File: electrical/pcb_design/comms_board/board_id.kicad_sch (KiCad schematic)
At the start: 10 parts

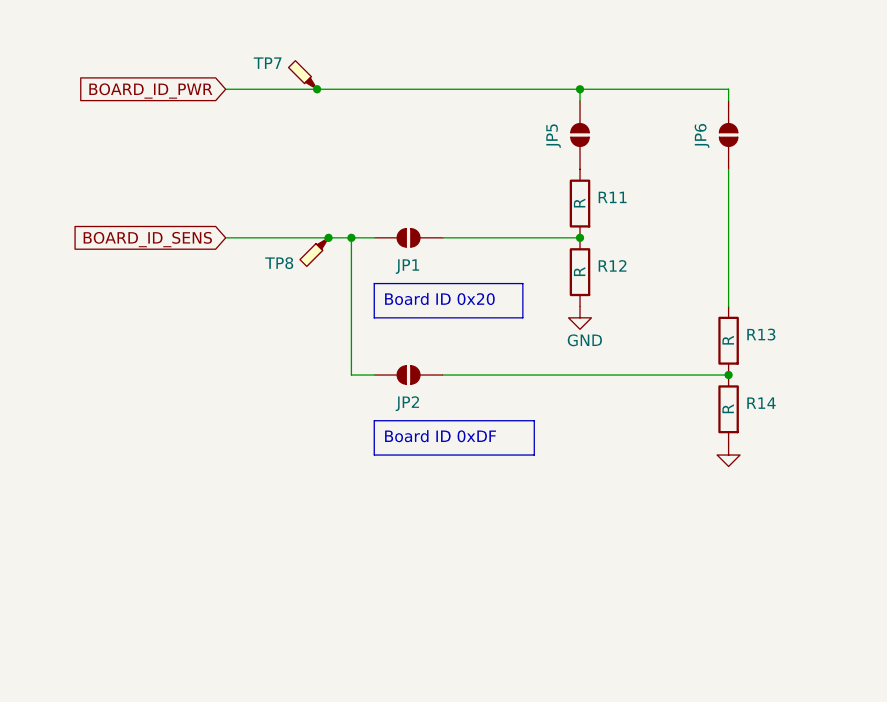
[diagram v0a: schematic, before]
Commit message: Create comms board for cheerful coffee edition based on magnetorquer control board
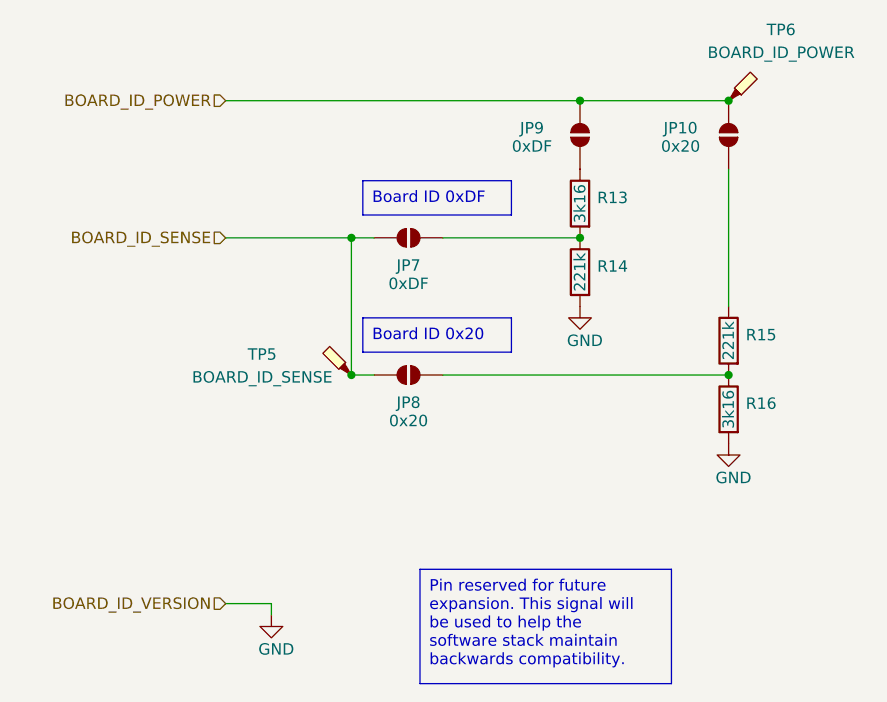
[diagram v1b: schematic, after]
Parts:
- removed JP2, JP6: SolderJumper_2_Open, Jumper:SolderJumper-2_P1.3mm_Open_RoundedPad1.0x1.5mm, symbol Jumper:SolderJumper_2_Open
- removed TP7, TP8: TestPoint_Probe, footprints:TestPoint_Pad_D2.5mm, symbol Connector:TestPoint_Probe
- added JP10, JP8: 0x20, Jumper:SolderJumper-2_P1.3mm_Open_RoundedPad1.0x1.5mm, symbol Jumper:SolderJumper_2_Open
- added TP5: BOARD_ID_SENSE, footprints:TestPoint_Pad_D1.5mm, symbol Connector:TestPoint_Probe
- added TP6: BOARD_ID_POWER, footprints:TestPoint_Pad_D1.5mm, symbol Connector:TestPoint_Probe
- JP7: renamed from JP1; value SolderJumper_2_Open -> 0xDF
- JP9: renamed from JP5; value SolderJumper_2_Open -> 0xDF
- R13: renamed from R11; value R -> 3k16; Active Y -> (none); MPN C11476 -> (none); Manufacturer Part Number 0402WGF1872TCE -> (none)
- R14: renamed from R12; value R -> 221k; Active Y -> (none); MPN C25914 -> (none); Manufacturer Part Number 0402WGF6191TCE -> (none)
- R15: renamed from R13; value R -> 221k; Active Y -> (none); MPN C25914 -> (none); Manufacturer Part Number 0402WGF6191TCE -> (none)
- R16: renamed from R14; value R -> 3k16; Active Y -> (none); MPN C11476 -> (none); Manufacturer Part Number 0402WGF1872TCE -> (none)
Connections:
- net at R15.1: now also JP10.2 (B)
- net at R15.2, R16.1: now also JP8.2 (B)
- net BOARD_ID_PWR renamed BOARD_ID_POWER
- net BOARD_ID_POWER: now also JP10.1 (A), TP6.1
- net BOARD_ID_SENS renamed BOARD_ID_SENSE
- net BOARD_ID_SENSE: now also JP8.1 (A), TP5.1

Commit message: Add missing part numbers to comms board.
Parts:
- R13, R16: Active (none) -> Y; Basic or Extended Component Basic -> Extended; MPN (none) -> C11462; Manufacturer Part Number (none) -> 0402WGF3161TCE
- R14, R15: Active (none) -> Y; Basic or Extended Component Basic -> Extended; MPN (none) -> C26998; Manufacturer Part Number (none) -> 0402WGF2213TCE
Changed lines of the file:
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@@
 			)
 		)
-		(property "Active" ""
+		(property "Active" "Y"
 			(at 163.83 95.25 0)
 			(effects
@@
 			)
 		)
-		(property "MPN" ""
+		(property "MPN" "C11462"
 			(at 163.83 95.25 0)
 			(effects
@@
 			)
 		)
-		(property "Manufacturer Part Number" ""
+		(property "Manufacturer Part Number" "0402WGF3161TCE"
 			(at 163.83 95.25 0)
 			(effects
@@
 			)
 		)
-		(property "Basic or Extended Component" "Basic"
+		(property "Basic or Extended Component" "Extended"
 			(at 163.83 95.25 0)
 			(effects
@@
 			)
 		)
-		(property "Active" ""
+		(property "Active" "Y"
 			(at 163.83 87.63 0)
 			(effects
@@
 			)
 		)
-		(property "MPN" ""
+		(property "MPN" "C26998"
 			(at 163.83 87.63 0)
 			(effects
@@
 			)
 		)
-		(property "Manufacturer Part Number" ""
+		(property "Manufacturer Part Number" "0402WGF2213TCE"
 			(at 163.83 87.63 0)
 			(effects
@@
 			)
 		)
-		(property "Basic or Extended Component" "Basic"
+		(property "Basic or Extended Component" "Extended"
 			(at 163.83 87.63 0)
 			(effects
@@
 			)
 		)
-		(property "Active" ""
+		(property "Active" "Y"
 			(at 147.32 80.01 0)
 			(effects
@@
 			)
 		)
-		(property "MPN" ""
+		(property "MPN" "C26998"
 			(at 147.32 80.01 0)
 			(effects
@@
 			)
 		)
-		(property "Manufacturer Part Number" ""
+		(property "Manufacturer Part Number" "0402WGF2213TCE"
 			(at 147.32 80.01 0)
 			(effects
@@
 			)
 		)
-		(property "Basic or Extended Component" "Basic"
+		(property "Basic or Extended Component" "Extended"
 			(at 147.32 80.01 0)
 			(effects
@@
 			)
 		)
-		(property "Active" ""
+		(property "Active" "Y"
 			(at 147.32 72.39 0)
 			(effects
@@
 			)
 		)
-		(property "MPN" ""
+		(property "MPN" "C11462"
 			(at 147.32 72.39 0)
 			(effects
@@
 			)
 		)
-		(property "Manufacturer Part Number" ""
+		(property "Manufacturer Part Number" "0402WGF3161TCE"
 			(at 147.32 72.39 0)
 			(effects
@@
 			)
 		)
-		(property "Basic or Extended Component" "Basic"
+		(property "Basic or Extended Component" "Extended"
 			(at 147.32 72.39 0)
 			(effects

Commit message: Select substitute resistor for out of stock component. Add a field to track the part number preferred when the board was designed.
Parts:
- R14, R15: Designed MPN (none) -> C26998; MPN C26998 -> C163479; Manufacturer UNI-ROYAL(Uniroyal Elec) -> YAGEO; Manufacturer Part Number 0402WGF2213TCE -> RC0402FR-07221KL
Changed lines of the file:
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@@
+			)
+		)
+		(property "Designed MPN" ""
+			(at 163.83 95.25 0)
+			(effects
+				(font
+					(size 1.27 1.27)
+				)
+				(hide yes)
 			)
 		)
@@
 			)
 		)
-		(property "MPN" "C26998"
+		(property "MPN" "C163479"
 			(at 163.83 87.63 0)
 			(effects
@@
 			)
 		)
-		(property "Manufacturer" "UNI-ROYAL(Uniroyal Elec)"
+		(property "Manufacturer" "YAGEO"
 			(at 163.83 87.63 0)
 			(effects
@@
 			)
 		)
-		(property "Manufacturer Part Number" "0402WGF2213TCE"
+		(property "Manufacturer Part Number" "RC0402FR-07221KL"
 			(at 163.83 87.63 0)
 			(effects
@@
 		)
 		(property "Arrow Price/Stock" ""
+			(at 163.83 87.63 0)
+			(effects
+				(font
+					(size 1.27 1.27)
+				)
+				(hide yes)
+			)
+		)
+		(property "Designed MPN" "C26998"
 			(at 163.83 87.63 0)
 			(effects
@@
 		)
 		(property "Arrow Price/Stock" ""
+			(at 163.83 64.77 0)
+			(effects
+				(font
+					(size 1.27 1.27)
+				)
+				(hide yes)
+			)
+		)
+		(property "Designed MPN" ""
 			(at 163.83 64.77 0)
 			(effects
@@
 			)
 		)
+		(property "Designed MPN" ""
+			(at 128.27 76.2 0)
+			(effects
+				(font
+					(size 1.27 1.27)
+				)
+				(hide yes)
+			)
+		)
 		(pin "2"
 		)
@@
 			)
 		)
+		(property "Designed MPN" ""
+			(at 163.83 60.96 0)
+			(effects
+				(font
+					(size 1.27 1.27)
+				)
+				(hide yes)
+			)
+		)
 		(pin "1"
 		)
@@
 			)
 		)
+		(property "Designed MPN" ""
+			(at 128.27 91.44 0)
+			(effects
+				(font
+					(size 1.27 1.27)
+				)
+				(hide yes)
+			)
+		)
 		(pin "2"
 		)
@@
 		)
 		(property "Arrow Price/Stock" ""
+			(at 121.92 91.44 0)
+			(effects
+				(font
+					(size 1.27 1.27)
+				)
+				(hide yes)
+			)
+		)
+		(property "Designed MPN" ""
 			(at 121.92 91.44 0)
 			(effects
@@
 			)
 		)
-		(property "MPN" "C26998"
+		(property "MPN" "C163479"
 			(at 147.32 80.01 0)
 			(effects
@@
 			)
 		)
-		(property "Manufacturer" "UNI-ROYAL(Uniroyal Elec)"
+		(property "Manufacturer" "YAGEO"
 			(at 147.32 80.01 0)
 			(effects
@@
 			)
 		)
-		(property "Manufacturer Part Number" "0402WGF2213TCE"
+		(property "Manufacturer Part Number" "RC0402FR-07221KL"
 			(at 147.32 80.01 0)
 			(effects
@@
 		)
 		(property "Arrow Price/Stock" ""
+			(at 147.32 80.01 0)
+			(effects
+				(font
+					(size 1.27 1.27)
+				)
+				(hide yes)
+			)
+		)
+		(property "Designed MPN" "C26998"
 			(at 147.32 80.01 0)
 			(effects
@@
 			)
 		)
+		(property "Designed MPN" ""
+			(at 147.32 72.39 0)
+			(effects
+				(font
+					(size 1.27 1.27)
+				)
+				(hide yes)
+			)
+		)
 		(pin "2"
 		)
@@
 			(at 147.32 64.77 0)
 			(effects
+				(font
+					(size 1.27 1.27)
+				)
+				(hide yes)
+			)
+		)
+		(property "Designed MPN" ""
+			(at 147.32 64.77 0)
+			(effects
